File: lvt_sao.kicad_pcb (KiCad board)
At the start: 2 copper layers, 1 part

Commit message: bla
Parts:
- added D1: LED, LED_SMD:LED_1210_3225Metric_Pad1.42x2.65mm_HandSolder, F.Cu at (90.2, 148.1)
- added D2: LED, LED_SMD:LED_1210_3225Metric_Pad1.42x2.65mm_HandSolder, F.Cu at (102.2, 148.1)
- added D3: LED, LED_SMD:LED_1210_3225Metric_Pad1.42x2.65mm_HandSolder, F.Cu at (140.9, 134.6)
- added D4: LED, LED_SMD:LED_1210_3225Metric_Pad1.42x2.65mm_HandSolder, F.Cu at (96.2, 148.1)
- added G***: LOGO, lvt:trailer, F.Cu at (128.7, 88.7)
- added LS1: Speaker, Connector_PinHeader_2.54mm:PinHeader_1x02_P2.54mm_Vertical, F.Cu at (106.0, 139.2)
- added Q1: MMBT3904, Package_TO_SOT_SMD:SOT-23, F.Cu at (128.6, 139.1)
- added R1: R, Resistor_SMD:R_1210_3225Metric_Pad1.30x2.65mm_HandSolder, F.Cu at (123.2, 139.0)
- added R2: R, Resistor_SMD:R_1210_3225Metric_Pad1.30x2.65mm_HandSolder, F.Cu at (111.3, 137.7)
- added R3: R, Resistor_SMD:R_1210_3225Metric_Pad1.30x2.65mm_HandSolder, F.Cu at (111.3, 141.9)
- added R4: R, Resistor_SMD:R_1210_3225Metric_Pad1.30x2.65mm_HandSolder, F.Cu at (117.2, 137.7)
- added R5: R, Resistor_SMD:R_1210_3225Metric_Pad1.30x2.65mm_HandSolder, F.Cu at (117.2, 141.9)
- added U1: DFR0299, lvt:MODULE_DFR0299, F.Cu at (149.3, 121.6)
- added U2: HC-SR501, HC-SR501:HC-SR501, F.Cu at (104.2, 123.1)
- added U3: ESP8266-01/ESP-01, esp01:XCVR_ESP8266-01_ESP-01, F.Cu at (130.0, 123.8)
- added X1: Badgelife_sao_connector_v169bis, badgelife_sao_v169bis:Badgelife-SAOv169-SAO-2x3, F.Cu at (95.4, 140.8)
- moved G*** 211.8 mm to (-65.8, 57.0)
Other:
- board outline added: 165.1 x 307.4 mm

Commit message: Cleaned up the board and added graphics
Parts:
- removed the G*** at (128.7, 88.7)
- added G***: LOGO, lvt:sturdy_trailer, F.Cu at (147.3, 116.8)
- moved R4 100.3 mm to (52.2, 61.4)
- moved D1 100.3 mm to (25.2, 71.8)
- moved R2 100.3 mm to (46.3, 61.4)
- moved D2 100.3 mm to (37.2, 71.8)
- moved D3 100.3 mm to (75.9, 58.3)
- moved D4 100.3 mm to (31.2, 71.8)
- moved LS1 100.3 mm to (41.0, 62.9)
- moved Q1 100.3 mm to (63.6, 62.8)
- moved R1 100.3 mm to (58.2, 62.6)
- moved R3 100.3 mm to (46.3, 65.6)
- moved R5 100.3 mm to (52.2, 65.6)
- moved U1 100.3 mm to (84.4, 45.2)
- moved U2 100.3 mm to (39.2, 46.8)
- moved X1 100.3 mm to (30.4, 64.5)
- moved U3 100.3 mm to (65.0, 47.4)
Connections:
- U1 pad 10: Net-(U1-Pad10) -> GND
- U1 pad 7: Net-(U1-Pad10) -> GND
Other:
- board size 165.1 x 307.4 mm -> 69 x 90.1 mm

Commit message: Made it pretty
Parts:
- added G***: LOGO, lvt:trailer_dither, F.Cu at (147.4, 116.6)

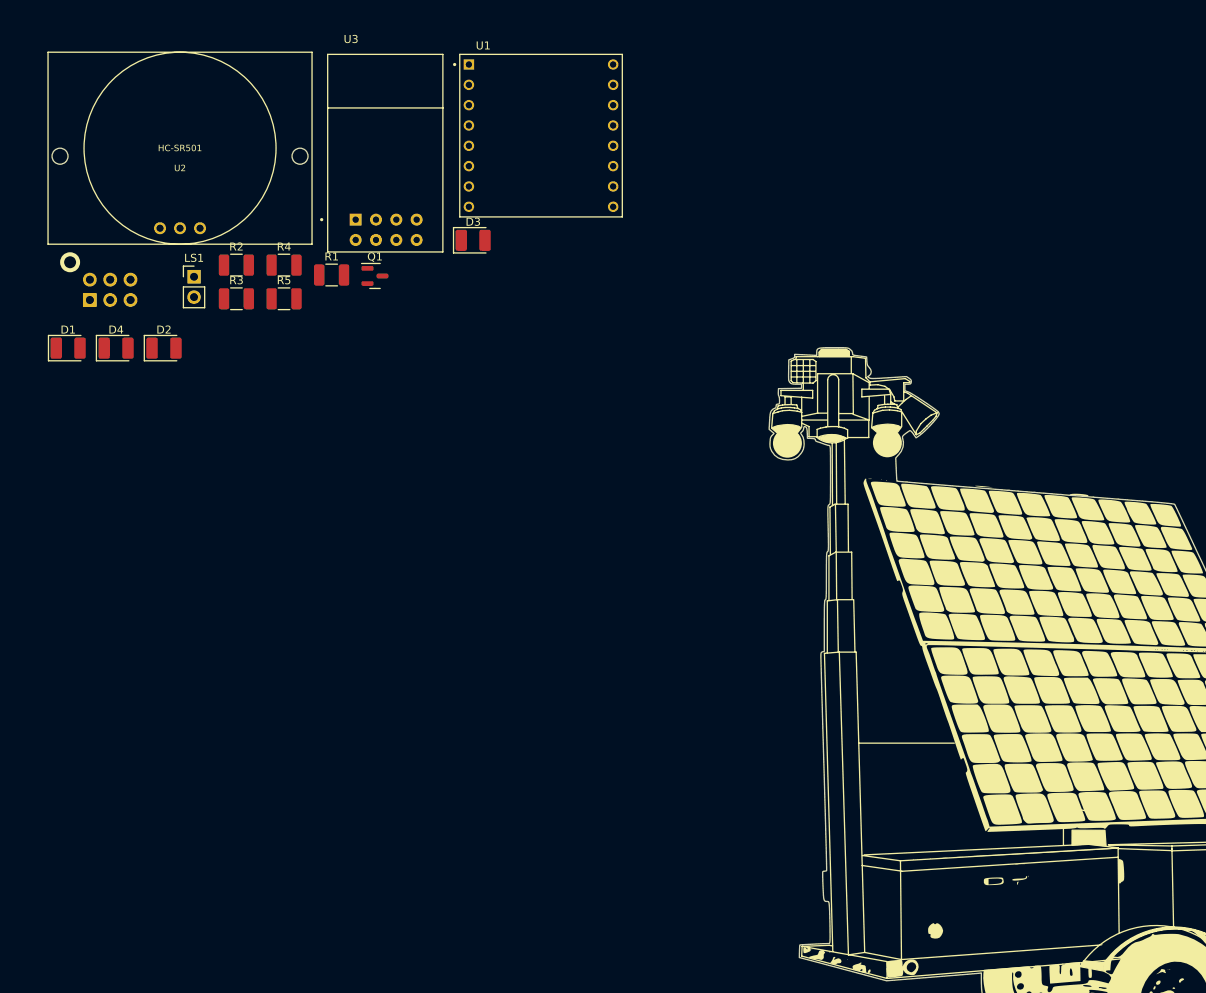
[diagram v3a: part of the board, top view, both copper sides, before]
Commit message: Components arranged and traces added
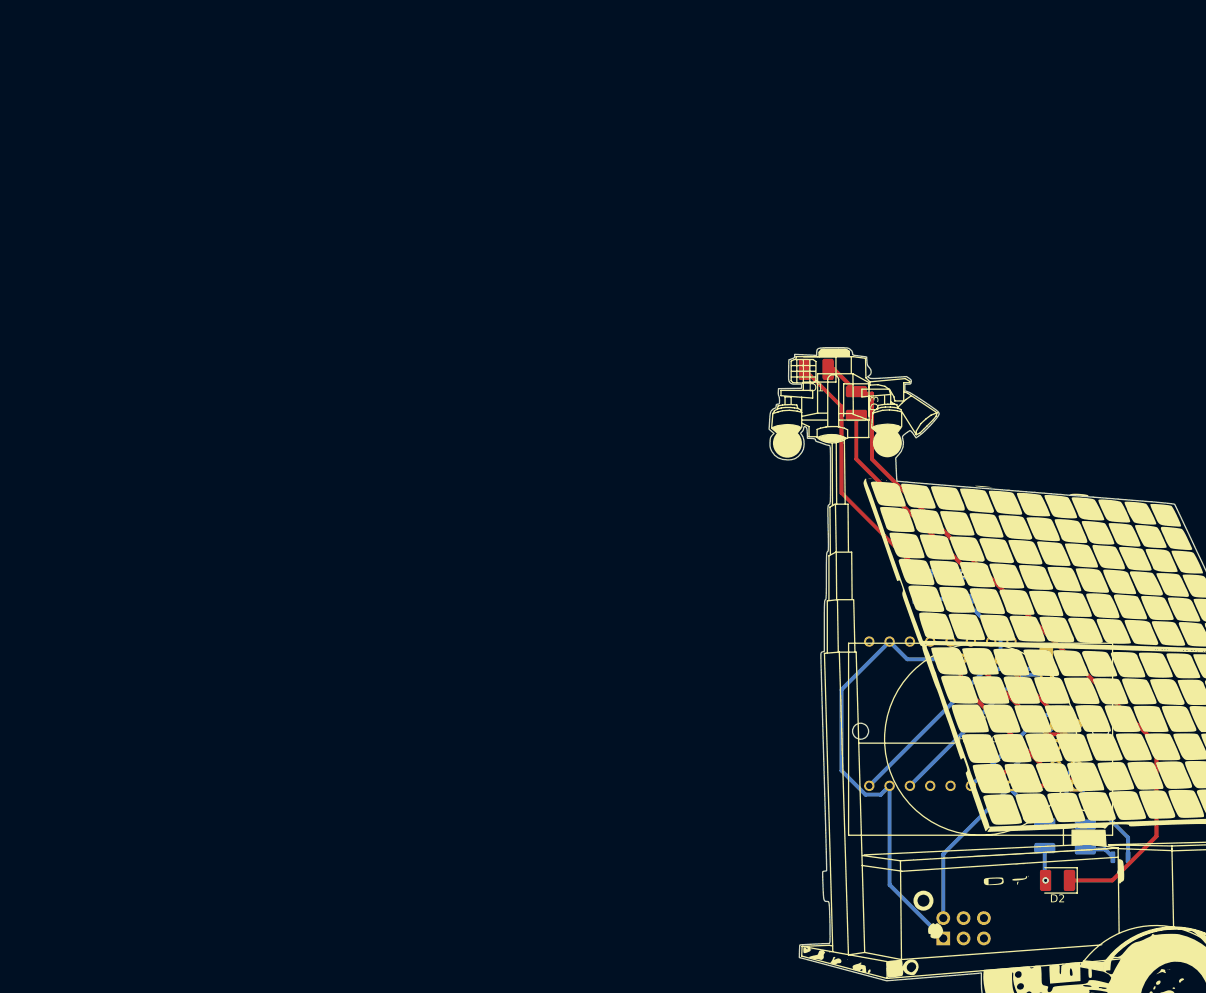
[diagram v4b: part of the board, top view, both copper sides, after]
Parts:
- removed D4: LED, LED_SMD:LED_1210_3225Metric_Pad1.42x2.65mm_HandSolder
- removed R5: R, Resistor_SMD:R_1210_3225Metric_Pad1.30x2.65mm_HandSolder
- LS1, Q1, R1, R2, R3, R4, U1, U3: moved to B.Cu
- moved X1 133.2 mm to (137.1, 144.3)
- moved D2 130.0 mm to (148.9, 138.3), turned to 180 degrees
- moved U2 124.4 mm to (139.3, 120.7), turned to 180 degrees
- moved R3 121.3 mm to (147.3, 132.7), turned to 90 degrees
- moved U3 120.8 mm to (159.6, 122.7), turned to 90 degrees
- moved Q1 118.7 mm to (156.8, 136.4), turned to -90 degrees
- moved R1 117.5 mm to (152.4, 132.9), turned to -90 degrees
- moved LS1 116.5 mm to (147.5, 110.1), turned to 180 degrees
- moved R2 94.7 mm to (132.1, 101.6), turned to -90 degrees
- moved R4 94.0 mm to (137.2, 101.6), turned to -90 degrees
- moved D1 93.6 mm to (118.8, 74.4), turned to 180 degrees
- moved U1 87.8 mm to (134.3, 117.5), turned to 90 degrees
- moved D3 52.1 mm to (123.8, 78.7), turned to -90 degrees
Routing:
- net GND: track 0.00 -> 92.4 mm
- net Net-(D1-Pad1): track 0.00 -> 90.0 mm, vias 0 -> 1
- net VCC: track 0.00 -> 62.0 mm
- net Net-(D1-Pad2): track 0.00 -> 31.7 mm, vias 0 -> 1
- net Net-(LS1-Pad1): track 0.00 -> 28.9 mm
- net Net-(D3-Pad2): track 0.00 -> 25.4 mm, vias 0 -> 1
- net Net-(LS1-Pad2): track 0.00 -> 22.8 mm
- net /ESP_UART_RX: track 0.00 -> 17.3 mm
- net /PIR_OUT: track 0.00 -> 17.0 mm
- net /ESP_UART_TX: track 0.00 -> 9.76 mm
- net /LED_TRIGGER: track 0.00 -> 8.87 mm
- net Net-(D2-Pad2): track 0.00 -> 4.08 mm, vias 0 -> 1
- net Net-(Q1-Pad1): track 0.00 -> 3.85 mm

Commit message: final revision before ordering
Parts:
- added J1: Conn_01x06_Male, Connector_PinHeader_2.54mm:PinHeader_1x06_P2.54mm_Vertical_SMD_Pin1Left, B.Cu at (131.0, 103.0)
- added R5: R, Resistor_SMD:R_1210_3225Metric_Pad1.30x2.65mm_HandSolder, B.Cu at (143.0, 122.0)
- added R6: R, Resistor_SMD:R_1210_3225Metric_Pad1.30x2.65mm_HandSolder, B.Cu at (161.0, 117.0)
- added R7: R, Resistor_SMD:R_1210_3225Metric_Pad1.30x2.65mm_HandSolder, B.Cu at (161.0, 123.0)
- G***: moved to B.Cu
- LS1: footprint Connector_PinHeader_2.54mm:PinHeader_1x02_P2.54mm_Vertical -> Connector_PinHeader_2.54mm:PinHeader_1x02_P2.54mm_Vertical_SMD_Pin1Left
- Q1: value MMBT3904 -> BC807
- moved G*** 223.0 mm to (153.0, 100.0), turned to 180 degrees
- moved LS1 30.0 mm to (127.0, 132.0), turned to -90 degrees
- moved R2 25.6 mm to (120.0, 79.0)
- moved R4 22.1 mm to (127.0, 82.0)
- moved R1 10.6 mm to (142.0, 131.0), turned to 180 degrees
- moved Q1 8.40 mm to (156.0, 128.0), turned to 180 degrees
- moved R3 1.44 mm to (148.0, 134.0)
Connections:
- D1 pad 1: Net-(D1-Pad1) -> GND
- D2 pad 1: Net-(D1-Pad1) -> GND
- D3 pad 1: Net-(D1-Pad1) -> GND
- Q1 pad 2: GND -> VCC
- Q1 pad 3: Net-(D1-Pad1) -> Net-(R2-Pad2)
- R1 pad 1: /LED_TRIGGER -> Net-(U3-Pad6)
- R1 pad 2: Net-(Q1-Pad1) -> VCC
- R2 pad 2: VCC -> Net-(R2-Pad2)
- R3 pad 2: VCC -> Net-(R2-Pad2)
- R4 pad 2: VCC -> Net-(R2-Pad2)
- U3 pad 2: /LED_TRIGGER -> /PIR_OUT
- U3 pad 3: /PIR_OUT -> /LED_TRIGGER
- U3 pad 6: unconnected-(U3-Pad6) -> Net-(U3-Pad6)
- U3 pad 7: unconnected-(U3-Pad7) -> /RESET
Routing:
- net Net-(R2-Pad2): track 0.00 -> 100.1 mm
- net GND: track 92.4 -> 0.00 mm
- net Net-(D1-Pad1): track 90.0 -> 0.00 mm, vias 1 -> 0
- net /LED_TRIGGER: track 8.87 -> 56.3 mm
- net /RESET: track 0.00 -> 37.7 mm
- net /ESP_UART_TX: track 9.76 -> 38.5 mm, vias 0 -> 1
- net /ESP_UART_RX: track 17.3 -> 45.6 mm, vias 0 -> 1
- net Net-(LS1-Pad1): track 28.9 -> 3.99 mm
- net VCC: track 62.0 -> 37.4 mm, vias 0 -> 3
- net Net-(D1-Pad2): track 31.7 -> 7.24 mm
- net Net-(D3-Pad2): track 25.4 -> 5.17 mm
- net Net-(LS1-Pad2): track 22.8 -> 8.07 mm
- net /PIR_OUT: track 17.0 -> 29.4 mm
- net Net-(U3-Pad6): track 0.00 -> 9.20 mm
- net /USB_D+: track 0.00 -> 8.47 mm
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- added copper zone on F.Cu, net GND
- added copper zone on B.Cu, net VCC
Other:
- board text added: "2022 - Design by: Mike Abbott github.com/furrysalamander furrysalamander@gmail.com Hunter Dalsing godfatherhaunter@gmail.com github.com/godfatherhunter"
